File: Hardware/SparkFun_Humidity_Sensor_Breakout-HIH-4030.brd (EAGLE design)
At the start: 19.1 x 7.6 mm, 3 parts, among them U1 HIH-4030SMD

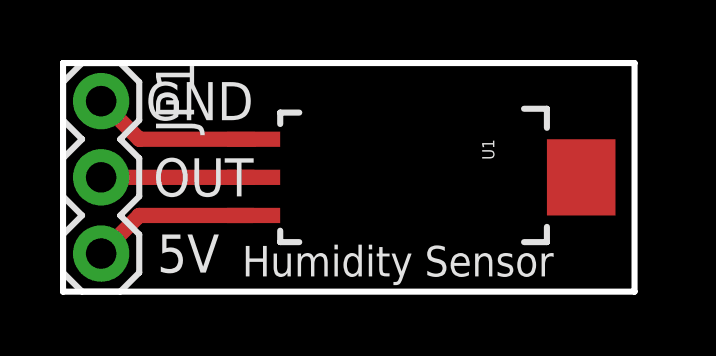
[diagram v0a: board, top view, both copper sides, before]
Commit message: added local fiducials
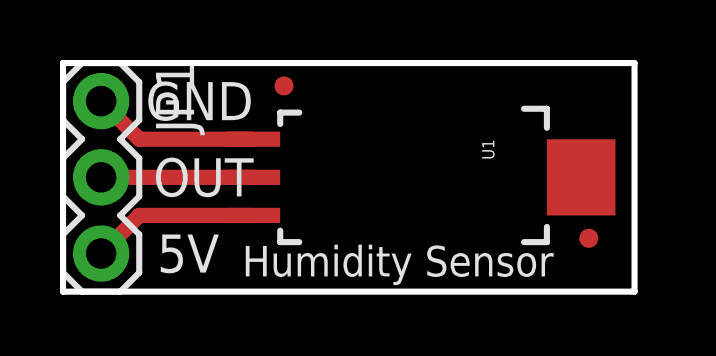
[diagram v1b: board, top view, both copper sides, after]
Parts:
- added FID1, FID2: FIDUCIALUFIDUCIAL, SparkFun-Aesthetics:MICRO-FIDUCIAL
